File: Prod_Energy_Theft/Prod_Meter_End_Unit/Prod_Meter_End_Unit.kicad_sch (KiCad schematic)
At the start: 31 parts, among them IC1 MP1584EN-LF-Z, J6 Jack-DC, J7 SS-52400-002, U1 TPS7A2033PDBVR, U3 BD00FC0WEFJ

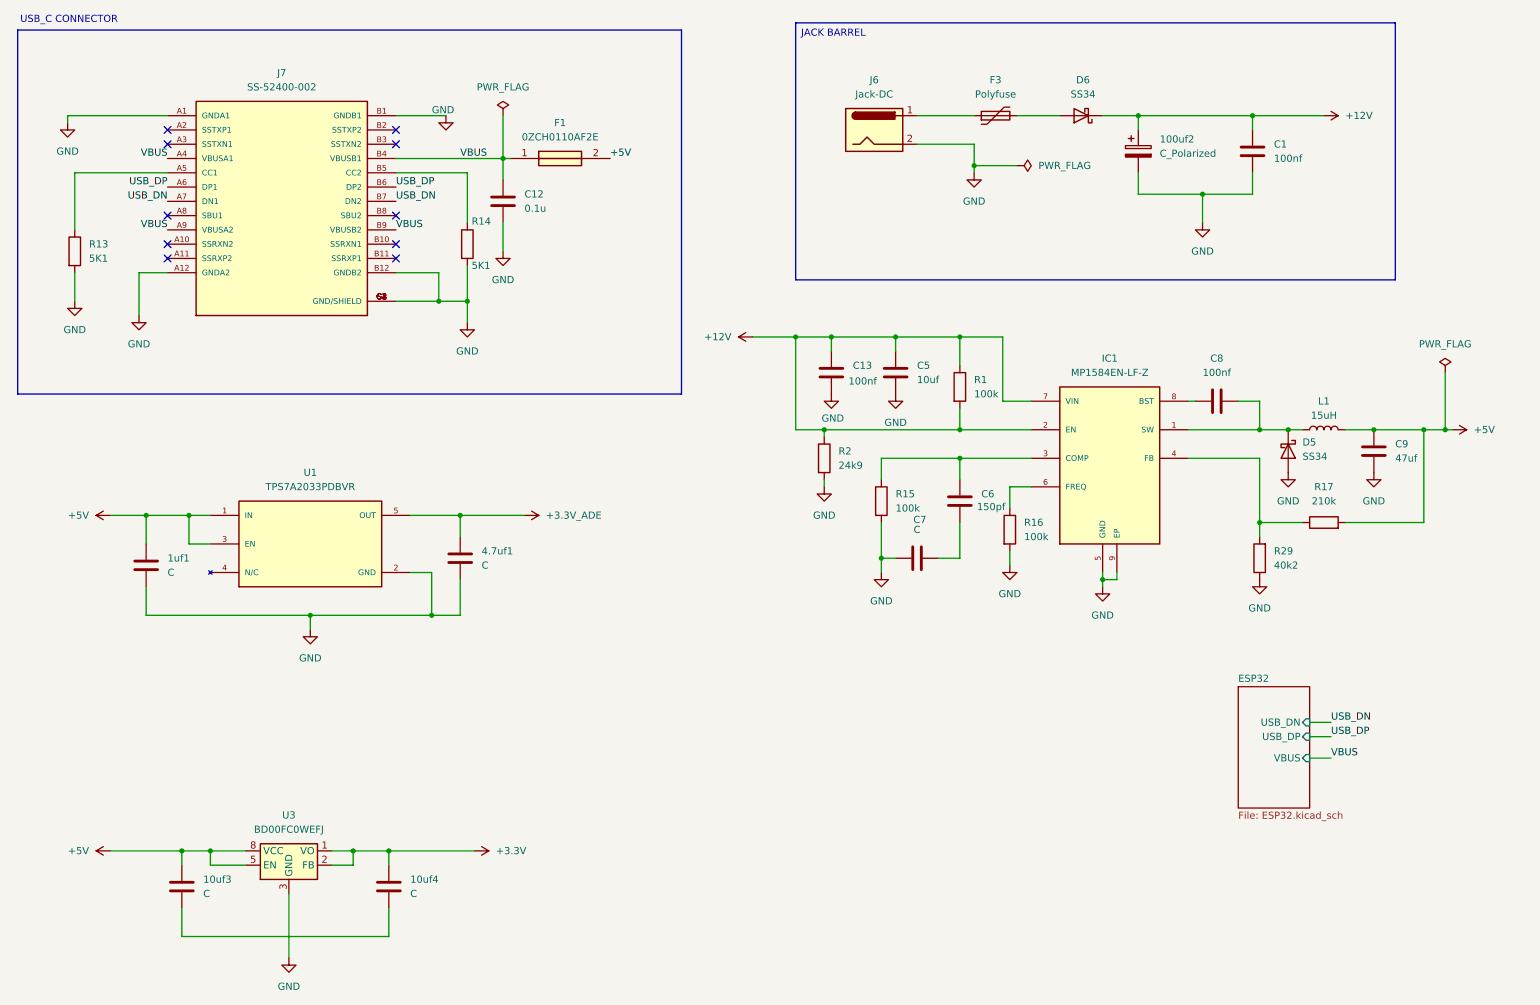
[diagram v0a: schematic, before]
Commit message: Chnages in power and ADE7816
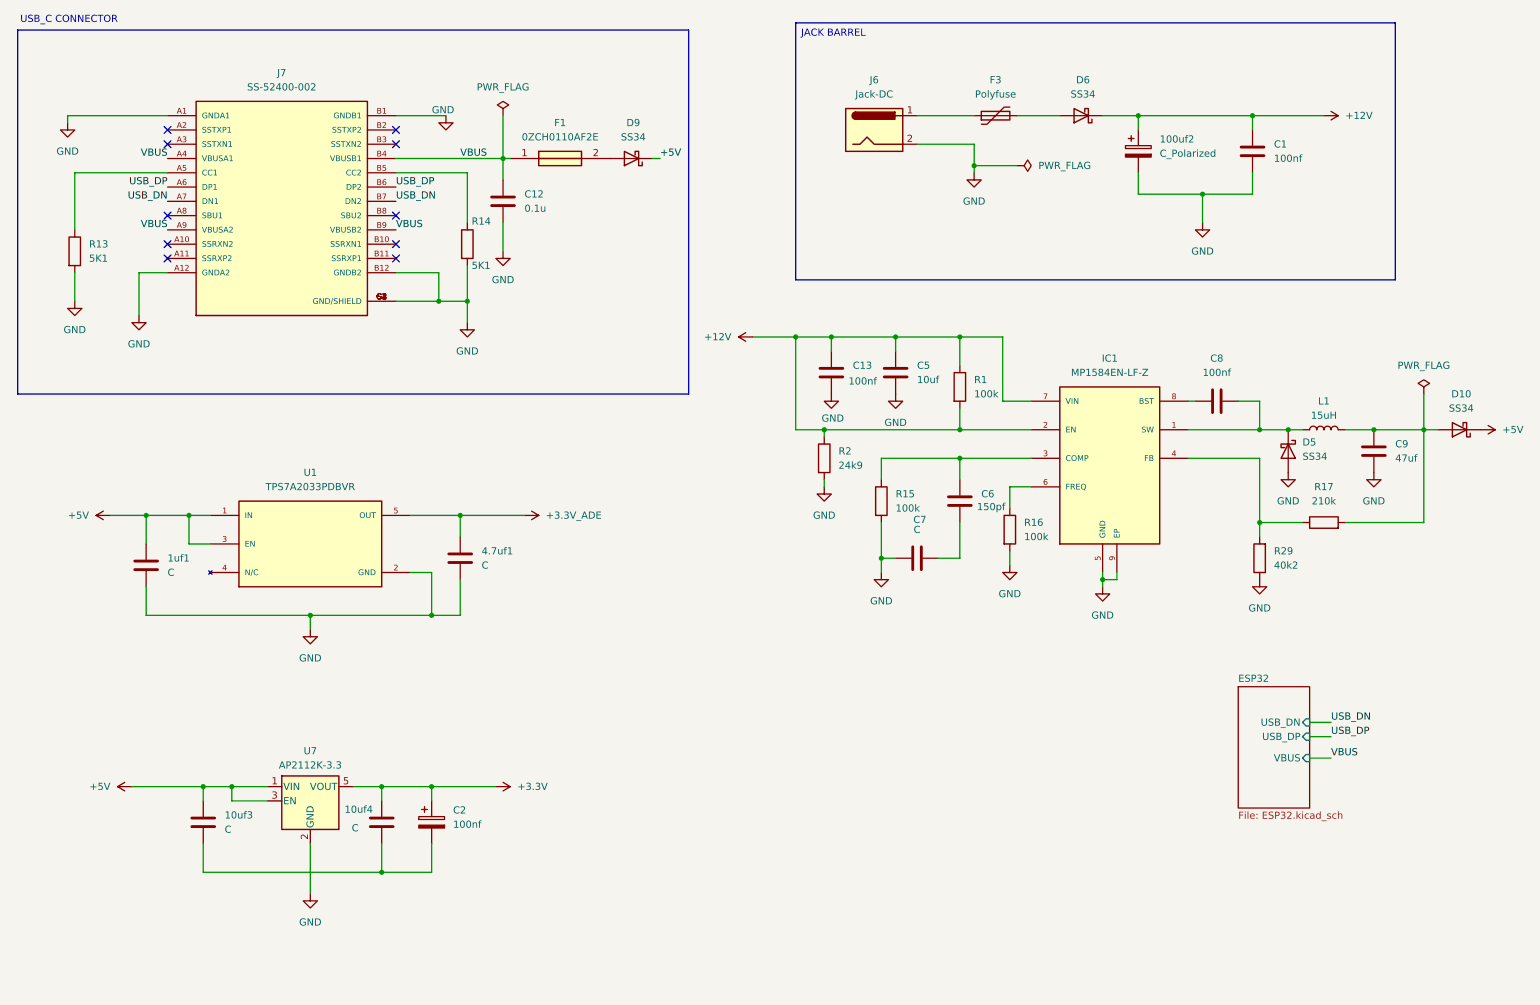
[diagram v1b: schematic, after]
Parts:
- removed U3: BD00FC0WEFJ, Package_SO:HTSOP-8-1EP_3.9x4.9mm_P1.27mm_EP2.4x3.2mm, symbol Regulator_Linear:BD00FC0WEFJ
- added C2: 100nf, symbol Device:C_Polarized
- added D10, D9: SS34, Diode_SMD:D_SMA, symbol Diode:SS34
- added U7: AP2112K-3.3, Package_TO_SOT_SMD:SOT-23-5, symbol Regulator_Linear:AP2112K-3.3
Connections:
- net +3.3V: now also C2.1, U7.5 (VOUT)
- net +5V: now also D10.1 (K), D9.1 (K), U7.1 (VIN), U7.3 (EN); no longer C9.1, F1.2, L1.2, R17.2
- net GND: now also U7.2 (GND)
- net at 10uf3.2, 10uf4.2: now also C2.2
- new net: C9.1, D10.2 (A), L1.2, R17.2
- new net: D9.2 (A), F1.2
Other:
- moved on the sheet: 10uf3, 10uf4

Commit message: PCB
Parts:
- C2: footprint (none) -> Capacitor_SMD:C_0805_2012Metric
- IC1: footprint MP1584EN-LF-Z:SOIC127P600X170-9N -> theftdetection:SOIC127P600X170-9N
- J7: footprint SS-52400-002:BELFUSE_SS-52400-002 -> theftdetection:BELFUSE_SS-52400-002
- U1: footprint TPS7A2033PDBVR:SOT95P280X145-5N -> theftdetection:SOT95P280X145-5N
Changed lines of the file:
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@@
 	)
 	(junction
+		(at 101.6 104.14)
+		(diameter 0)
+		(color 0 0 0 0)
+	)
+	(junction
 		(at 49.53 152.4)
 		(diameter 0)
@@
 	)
 	(junction
+		(at 41.91 152.4)
+		(diameter 0)
+		(color 0 0 0 0)
+	)
+	(junction
 		(at 236.22 33.02)
 		(diameter 0)
@@
 	(wire
 		(pts
+			(xy 101.6 97.79) (xy 101.6 104.14)
+		)
+		(stroke
+			(width 0)
+			(type default)
+		)
+	)
+	(wire
+		(pts
 			(xy 184.15 85.09) (xy 184.15 88.9)
 		)
@@
 	(wire
 		(pts
-			(xy 36.83 152.4) (xy 49.53 152.4)
+			(xy 36.83 152.4) (xy 41.91 152.4)
 		)
 		(stroke
@@
 	(wire
 		(pts
+			(xy 41.91 152.4) (xy 49.53 152.4)
+		)
+		(stroke
+			(width 0)
+			(type default)
+		)
+	)
+	(wire
+		(pts
 			(xy 237.49 83.82) (xy 237.49 88.9)
 		)
@@
 	(wire
 		(pts
+			(xy 41.91 144.78) (xy 41.91 152.4)
+		)
+		(stroke
+			(width 0)
+			(type default)
+		)
+	)
+	(wire
+		(pts
 			(xy 68.58 121.92) (xy 68.58 124.46)
 		)
@@
 	(wire
 		(pts
+			(xy 101.6 104.14) (xy 106.68 104.14)
+		)
+		(stroke
+			(width 0)
+			(type default)
+		)
+	)
+	(wire
+		(pts
 			(xy 252.73 88.9) (xy 257.81 88.9)
 		)
@@
 	(wire
 		(pts
-			(xy 95.25 104.14) (xy 106.68 104.14)
+			(xy 95.25 104.14) (xy 101.6 104.14)
 		)
 		(stroke
@@
 	)
 	(symbol
+		(lib_id "power:PWR_FLAG")
+		(at 41.91 144.78 0)
+		(unit 1)
+		(exclude_from_sim no)
+		(in_bom yes)
+		(on_board yes)
+		(dnp no)
+		(fields_autoplaced yes)
+		(property "Reference" "#FLG08"
+			(at 41.91 142.875 0)
+			(effects
+				(font
+					(size 1.27 1.27)
+				)
+				(hide yes)
+			)
+		)
+		(property "Value" "PWR_FLAG"
+			(at 41.91 139.7 0)
+			(effects
+				(font
+					(size 1.27 1.27)
+				)
+			)
+		)
+		(property "Footprint" ""
+			(at 41.91 144.78 0)
+			(effects
+				(font
+					(size 1.27 1.27)
+				)
+				(hide yes)
+			)
+		)
+		(property "Datasheet" "~"
+			(at 41.91 144.78 0)
+			(effects
+				(font
+					(size 1.27 1.27)
+				)
+				(hide yes)
+			)
+		)
+		(property "Description" "Special symbol for telling ERC where power comes from"
+			(at 41.91 144.78 0)
+			(effects
+				(font
+					(size 1.27 1.27)
+				)
+				(hide yes)
+			)
+		)
+		(pin "1"
+		)
+		(instances
+			(project "Prod_Meter_End_Unit"
+				(path "/5bca34b5-540d-46d7-a7e3-e92e31ef4c0b"
+					(reference "#FLG08")
+					(unit 1)
+				)
+			)
+		)
+	)
+	(symbol
 		(lib_id "Device:R")
 		(at 193.04 106.68 0)
@@
 			)
 		)
-		(property "Footprint" "SS-52400-002:BELFUSE_SS-52400-002"
+		(property "Footprint" "theftdetection:BELFUSE_SS-52400-002"
 			(at 63.5 48.26 0)
 			(effects
@@
 	(symbol
 		(lib_id "power:PWR_FLAG")
+		(at 101.6 97.79 0)
+		(unit 1)
+		(exclude_from_sim no)
+		(in_bom yes)
+		(on_board yes)
+		(dnp no)
+		(fields_autoplaced yes)
+		(property "Reference" "#FLG09"
+			(at 101.6 95.885 0)
+			(effects
+				(font
+					(size 1.27 1.27)
+				)
+				(hide yes)
+			)
+		)
+		(property "Value" "PWR_FLAG"
+			(at 101.6 92.71 0)
+			(effects
+				(font
+					(size 1.27 1.27)
+				)
+			)
+		)
+		(property "Footprint" ""
+			(at 101.6 97.79 0)
+			(effects
+				(font
+					(size 1.27 1.27)
+				)
+				(hide yes)
+			)
+		)
+		(property "Datasheet" "~"
+			(at 101.6 97.79 0)
+			(effects
+				(font
+					(size 1.27 1.27)
+				)
+				(hide yes)
+			)
+		)
+		(property "Description" "Special symbol for telling ERC where power comes from"
+			(at 101.6 97.79 0)
+			(effects
+				(font
+					(size 1.27 1.27)
+				)
+				(hide yes)
+			)
+		)
+		(pin "1"
+		)
+		(instances
+			(project "Prod_Meter_End_Unit"
+				(path "/5bca34b5-540d-46d7-a7e3-e92e31ef4c0b"
+					(reference "#FLG09")
+					(unit 1)
+				)
+			)
+		)
+	)
+	(symbol
+		(lib_id "power:PWR_FLAG")
 		(at 102.87 33.02 0)
 		(unit 1)
@@
 			)
 		)
-		(property "Footprint" "MP1584EN-LF-Z:SOIC127P600X170-9N"
+		(property "Footprint" "theftdetection:SOIC127P600X170-9N"
 			(at 196.85 83.82 0)
 			(effects
@@
 			)
 		)
-		(property "Footprint" ""
+		(property "Footprint" "Capacitor_SMD:C_0805_2012Metric"
 			(at 91.1352 162.56 0)
 			(effects
@@
 			)
 		)
-		(property "Footprint" "TPS7A2033PDBVR:SOT95P280X145-5N"
+		(property "Footprint" "theftdetection:SOT95P280X145-5N"
 			(at 68.58 109.22 0)
 			(effects

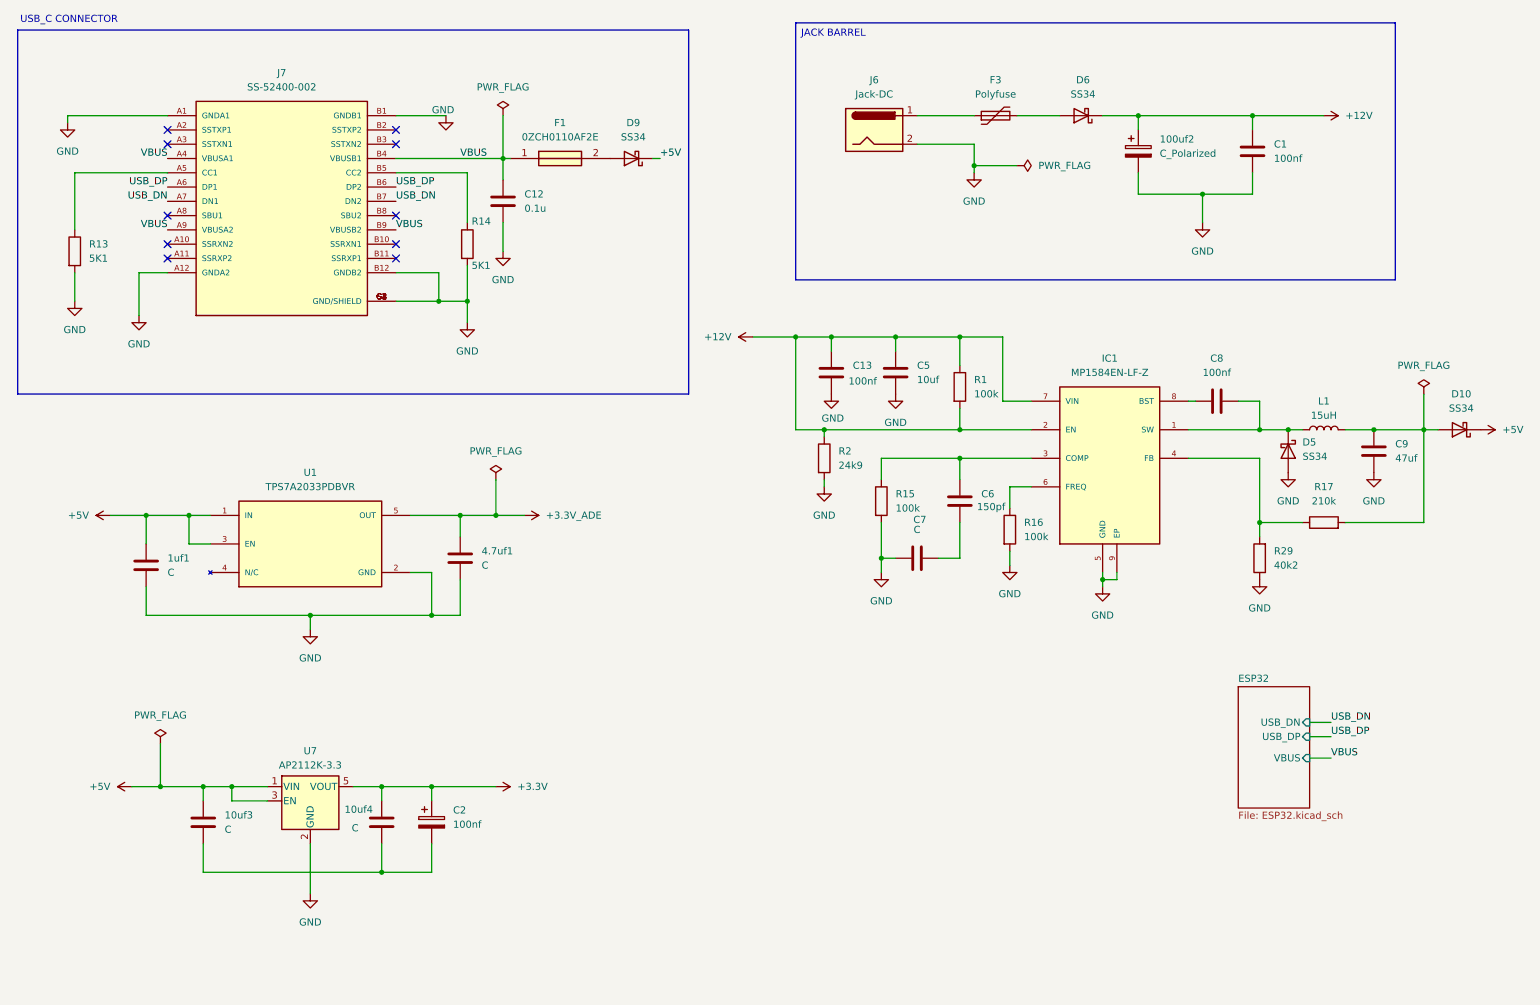
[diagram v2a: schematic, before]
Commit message: update in BOM list
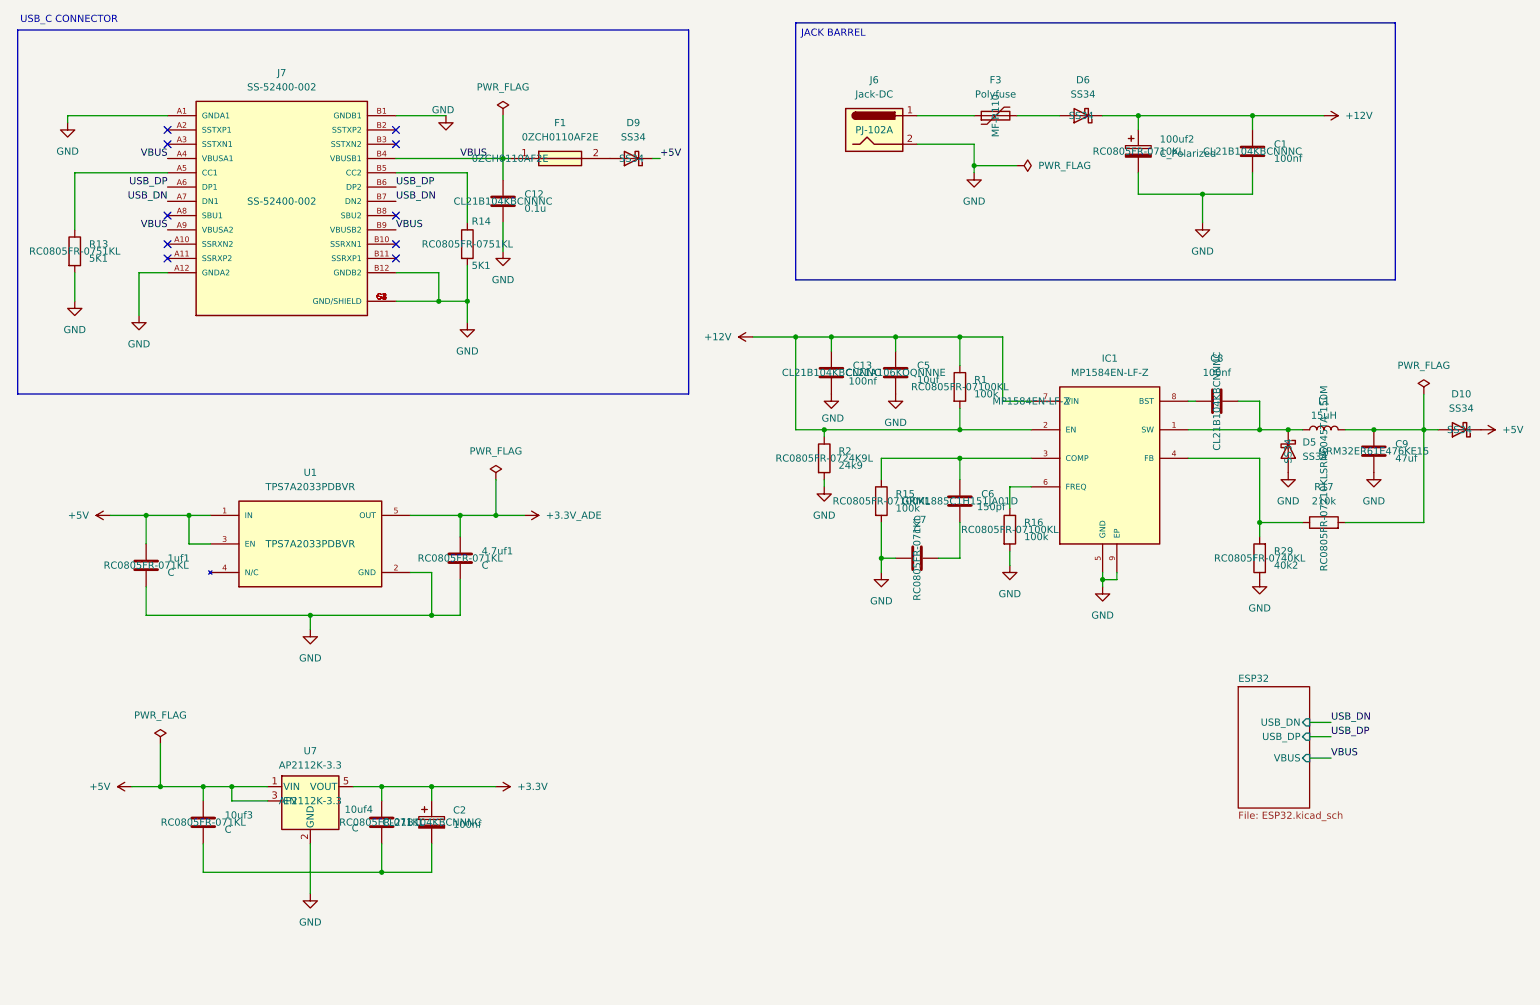
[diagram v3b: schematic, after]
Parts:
- 100uf2: Part Number (none) -> RC0805FR-0710KL
- 10uf3, 10uf4, 1uf1, 4.7uf1, C7: Part Number (none) -> RC0805FR-071KL
- C1, C12, C13, C2, C8: Part Number (none) -> CL21B104KBCNNNC
- C5: Part Number (none) -> CL21A106KOQNNNE
- C6: Part Number (none) -> GRM1885C1H151JA01D
- C9: Part Number (none) -> GRM32ER61E476KE15
- D10, D5, D6, D9: Part Number (none) -> SS34
- F1: Part Number (none) -> 0ZCH0110AF2E
- F3: Part Number (none) -> MF-R110
- IC1: Part Number (none) -> MP1584EN-LF-Z
- J6: Part Number (none) -> PJ-102A
- J7: Part Number (none) -> SS-52400-002
- L1: Part Number (none) -> SRN6045TA-150M
- R1, R15, R16: Part Number (none) -> RC0805FR-07100KL
- R13, R14: Part Number (none) -> RC0805FR-0751KL
- R17: Part Number (none) -> RC0805FR-07210KL
- R2: Part Number (none) -> RC0805FR-0724K9L
- R29: Part Number (none) -> RC0805FR-0740KL
- U1: Part Number (none) -> TPS7A2033PDBVR
- U7: Part Number (none) -> AP2112K-3.3
